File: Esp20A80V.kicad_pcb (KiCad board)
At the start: 2 copper layers, 75 x 29 mm, 19 parts, among them J1 dcdc, J4 I2C/Uart, Q1 SI2305, SW1 3x button, U1 tft + touch + sd card, U3 20A 80V dcdc, U4 Wemos S2 Mini

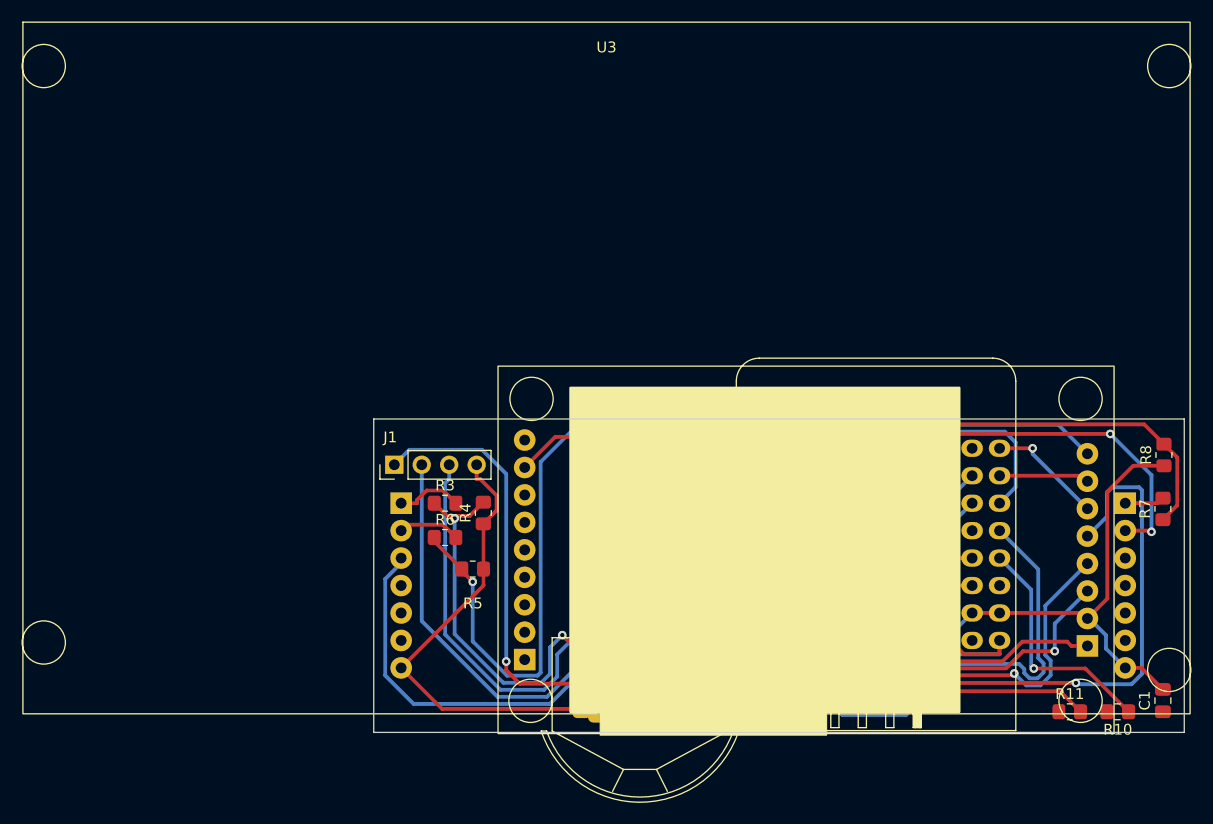
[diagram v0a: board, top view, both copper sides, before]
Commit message: footsprints verified and sd card added
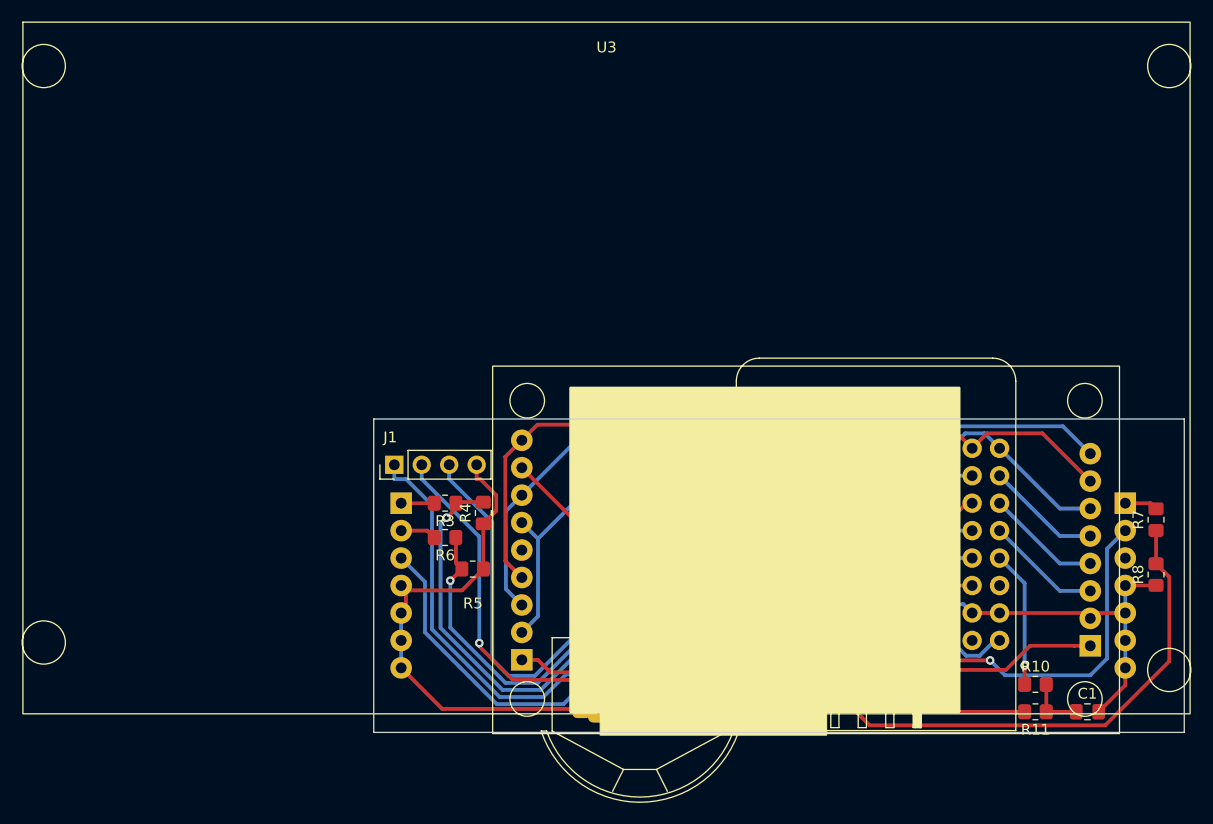
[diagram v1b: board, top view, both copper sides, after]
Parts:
- U1: value tft + touch + sd card -> spi tft with touch (+ sd card)
- moved Q1 27.5 mm to (152.7, 94.3), turned to 180 degrees
- moved R2 26.7 mm to (155.2, 97.8), turned to 180 degrees
- moved R1 19.1 mm to (148.6, 94.0), turned to -90 degrees
- moved R8 11.1 mm to (176.5, 101.6)
- moved R10 8.03 mm to (165.4, 111.8), turned to 0 degrees
- moved C1 7.06 mm to (170.2, 114.3), turned to 0 degrees
- moved R11 3.17 mm to (165.4, 114.3), turned to 180 degrees
- moved R7 1.18 mm to (176.5, 96.5)
- turned R3 to 180 degrees
- turned R6 to 180 degrees
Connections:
- net Net-(R7-Pad1) renamed iVout
- net Vin renamed Net-(U3-V_in)
- net Vout renamed Net-(U3-V_out)
- R2 pad 1: Net-(R2-Pad1) -> led
- R3 pad 1: Net-(R3-Pad1) -> enable
- R3 pad 2: enable -> Net-(U3-enable)
- R4 pad 2: Net-(R3-Pad1) -> enable
- R5 pad 2: Net-(R5-Pad2) -> iVin
- R6 pad 1: Net-(R5-Pad2) -> iVin
- SW1 pad 1: Net-(SW1-up) -> up
- SW1 pad 2: Net-(SW1-push) -> push
- SW1 pad 3: Net-(SW1-down) -> down
- U1 pad 10: unconnected-(U1-SD_MOSI-Pad10) -> MISO
- U1 pad 11: unconnected-(U1-SD_MISO-Pad11) -> MOSI
- U1 pad 12: unconnected-(U1-SD_SCK-Pad12) -> SCK
- U1 pad 14: unconnected-(U1-T_DO-Pad14) -> MISO
- U1 pad 15: unconnected-(U1-T_DIN-Pad15) -> MOSI
- U1 pad 16: Net-(U1-T_CS) -> T_CS
- U1 pad 17: unconnected-(U1-T_CLK-Pad17) -> SCK
- U1 pad 3: Net-(U1-CS) -> CS
- U1 pad 4: Net-(U1-RESET) -> RESET
- U1 pad 5: Net-(U1-A0) -> A0
- U1 pad 6: Net-(U1-SDA) -> MOSI
- U1 pad 7: Net-(U1-SCK) -> SCK
- U1 pad 9: unconnected-(U1-SD_CS-Pad9) -> SD_CS
- U3 pad 1: enable -> Net-(U3-enable)
- U3 pad 11: unconnected-(U3-GND-Pad11) -> GND
- U3 pad 12: unconnected-(U3-GND-Pad12) -> GND
- U3 pad 13: unconnected-(U3-GND-Pad13) -> GND
- U3 pad 4: unconnected-(U3-GND-Pad4) -> GND
- U3 pad 5: unconnected-(U3-GND-Pad5) -> GND
- U3 pad 6: unconnected-(U3-GND-Pad6) -> GND
- U4 pad 1: Net-(R5-Pad2) -> unconnected-(U4-Pad1)
- U4 pad 10: Net-(SW1-up) -> unconnected-(U4-Pad10)
- U4 pad 11: Net-(U1-CS) -> push
- U4 pad 12: Net-(R2-Pad1) -> up
- U4 pad 13: Net-(SW1-push) -> SD_CS
- U4 pad 14: Net-(SW1-down) -> mode
- U4 pad 21: mode -> SDA
- U4 pad 3: unconnected-(U4-Pad3) -> iVin
- U4 pad 33: Net-(R3-Pad1) -> CS
- U4 pad 34: unconnected-(U4-Pad34) -> SCL
- U4 pad 35: Net-(U1-T_CS) -> RESET
- U4 pad 36: SDA -> led
- U4 pad 37: Net-(U1-SCK) -> A0
- U4 pad 38: SCL -> MISO
- U4 pad 39: Net-(U1-SDA) -> MOSI
- U4 pad 40: unconnected-(U4-Pad40) -> SCK
- U4 pad 5: unconnected-(U4-Pad5) -> enable
- U4 pad 7: Net-(U1-A0) -> T_CS
- U4 pad 9: Net-(U1-RESET) -> down
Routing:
- net Net-(R3-Pad1): track 97.6 -> 0.00 mm, vias 3 -> 0
- net Net-(U1-A0): track 78.3 -> 0.00 mm, vias 1 -> 0
- net MOSI: track 0.00 -> 70.9 mm
- net SCK: track 0.00 -> 70.5 mm
- net Net-(R5-Pad2): track 62.6 -> 0.00 mm, vias 2 -> 0
- net MISO: track 0.00 -> 57.3 mm
- net Net-(U1-T_CS): track 54.3 -> 0.00 mm, vias 1 -> 0
- net Net-(U1-RESET): track 53.2 -> 0.00 mm, vias 1 -> 0
- net iVin: track 0.00 -> 47.0 mm, vias 0 -> 1
- net enable: track 6.21 -> 53.1 mm, vias 0 -> 1
- net Net-(U1-CS): track 44.0 -> 0.00 mm, vias 1 -> 0
- net Net-(Q1-S): track 51.7 -> 20.9 mm
- net SD_CS: track 0.00 -> 30.5 mm, vias 0 -> 1
- net iVout: track 46.3 -> 74.7 mm, vias 0 -> 1
- net mode: track 82.3 -> 54.3 mm, vias 3 -> 0
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
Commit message: better circuit
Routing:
- net GND: track 118.4 -> 146.1 mm
- net iVout: track 74.7 -> 47.6 mm, vias 1 -> 0
- net enable: track 53.1 -> 36.0 mm, vias 1 -> 0
- net +5V: track 96.6 -> 102.8 mm
- net SCK: track 70.5 -> 75.7 mm
- net MISO: track 57.3 -> 62.5 mm
- net DAC in: track 64.3 -> 61.8 mm
- net mode: track 54.3 -> 52.1 mm
- net Iout: track 54.4 -> 55.7 mm, vias 1 -> 0
- net Net-(U1-VCC): track 33.3 -> 32.2 mm
- net Net-(Q1-S): track 20.9 -> 20.1 mm, vias 1 -> 0
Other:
- board size 75 x 29 mm -> 75 x 30 mm

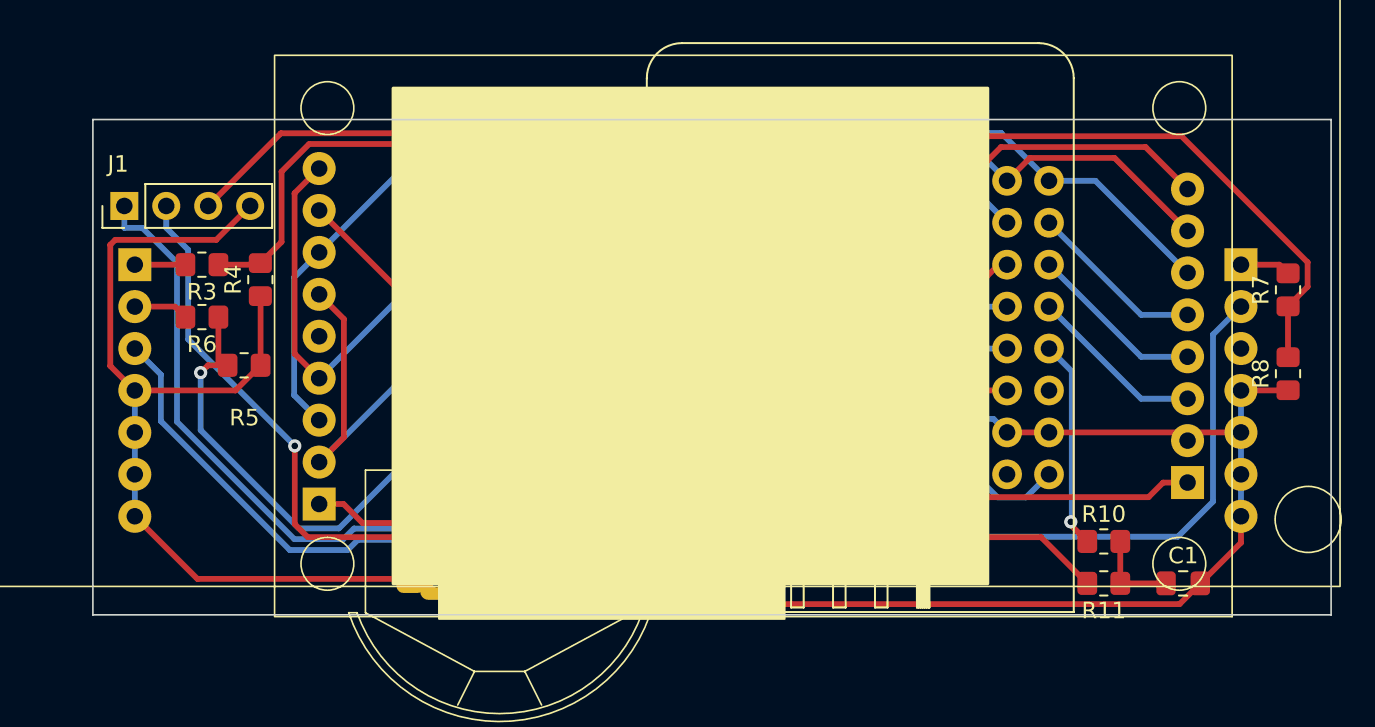
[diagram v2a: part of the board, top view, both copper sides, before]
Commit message: jst ph2.0 instead of dupont female
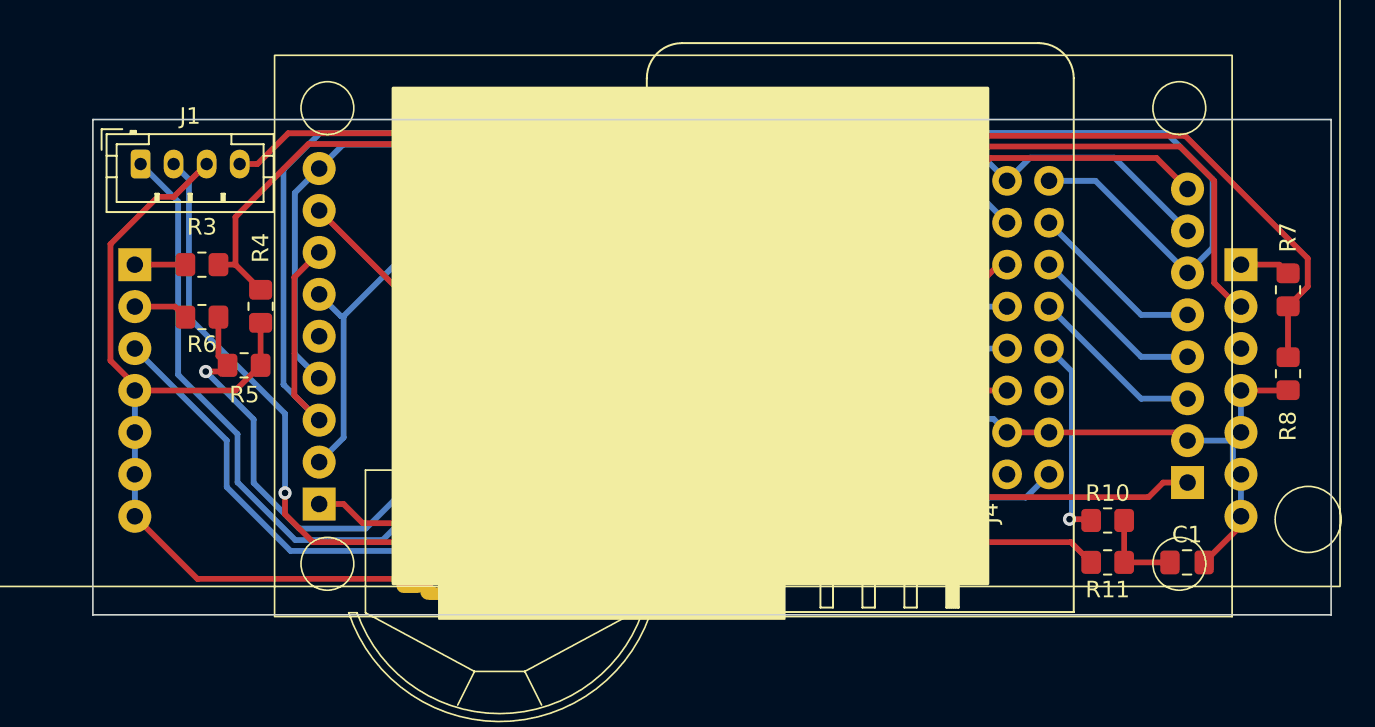
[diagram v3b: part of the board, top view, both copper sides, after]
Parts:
- added J2: free, Connector_PinHeader_2.54mm:PinHeader_1x06_P2.54mm_Horizontal, F.Cu at (144.8, 106.7)
- J1: footprint Connector_PinHeader_2.54mm:PinHeader_1x04_P2.54mm_Vertical -> Connector_JST:JST_PH_B4B-PH-K_1x04_P2.00mm_Vertical
- moved J1 2.72 mm to (107.0, 88.9), turned to 0 degrees
- moved J4 1.78 mm to (156.2, 105.7)
- moved R4 1.62 mm to (114.3, 97.5)
- moved R10 1.29 mm to (165.6, 110.5)
- moved C1 1.29 mm to (170.4, 113.0)
- moved R11 1.29 mm to (165.6, 113.0)
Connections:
- net DAC in renamed DAC_in
- net Net-(U1-VCC) renamed 3.3V
- J1 pad 3: +5V -> GND
- J1 pad 4: GND -> +5V
- U4 pad 1: unconnected-(U4-Pad1) -> iVout
- U4 pad 10: unconnected-(U4-Pad10) -> F1
- U4 pad 2: iVout -> Iout
- U4 pad 4: Iout -> F4
- U4 pad 6: unconnected-(U4-Pad6) -> F3
- U4 pad 8: unconnected-(U4-Pad8) -> F2
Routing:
- net +5V: track 102.8 -> 68.2 mm, vias 1 -> 0
- net MOSI: track 70.5 -> 102.8 mm
- net Iout: track 55.7 -> 41.5 mm, vias 0 -> 1
- net GND: track 146.1 -> 134.1 mm
- net SCK: track 75.7 -> 70.5 mm
- net MISO: track 62.5 -> 57.3 mm
- net F3: track 0.00 -> 3.47 mm
- net F1: track 0.00 -> 3.47 mm
- net F4: track 0.00 -> 3.47 mm
- net F2: track 0.00 -> 3.47 mm
- net 3.3V: track 32.2 -> 34.9 mm
- net DAC_out: track 72.0 -> 74.0 mm
- net SDA: track 12.5 -> 10.7 mm
- net SCL: track 16.1 -> 14.3 mm
- net mode: track 52.1 -> 53.6 mm, vias 0 -> 1
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
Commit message: update
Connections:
- J1 pad 1: mode -> DAC_out
- J1 pad 2: DAC_out -> mode
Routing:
- net GND: track 134.1 -> 0.00 mm
- net MOSI: track 102.8 -> 0.00 mm
- net DAC_out: track 74.0 -> 0.00 mm, vias 1 -> 0
- net SCK: track 70.5 -> 0.00 mm
- net +5V: track 68.2 -> 0.00 mm
- net DAC_in: track 60.4 -> 0.00 mm, vias 1 -> 0
- net MISO: track 57.3 -> 0.00 mm
- net mode: track 53.6 -> 0.00 mm, vias 1 -> 0
- net iVin: track 46.7 -> 0.00 mm, vias 1 -> 0
- net iVout: track 46.7 -> 0.00 mm, vias 1 -> 0
- net Iout: track 41.5 -> 0.00 mm, vias 1 -> 0
- net enable: track 37.3 -> 0.00 mm
- net 3.3V: track 34.9 -> 0.00 mm
- net SD_CS: track 30.4 -> 0.00 mm
- net T_CS: track 23.8 -> 0.00 mm
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
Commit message: update
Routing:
- net GND: track 0.00 -> 133.9 mm
- net MOSI: track 0.00 -> 111.4 mm, vias 0 -> 1
- net +5V: track 0.00 -> 98.4 mm, vias 0 -> 1
- net DAC_out: track 0.00 -> 83.0 mm
- net SCK: track 0.00 -> 74.5 mm
- net DAC_in: track 0.00 -> 60.1 mm, vias 0 -> 1
- net MISO: track 0.00 -> 57.9 mm
- net iVin: track 0.00 -> 47.8 mm, vias 0 -> 1
- net iVout: track 0.00 -> 46.7 mm
- net mode: track 0.00 -> 43.5 mm, vias 0 -> 1
- net Iout: track 0.00 -> 41.5 mm
- net enable: track 0.00 -> 37.8 mm
- net 3.3V: track 0.00 -> 34.9 mm
- net SD_CS: track 0.00 -> 31.1 mm
- net T_CS: track 0.00 -> 23.9 mm
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
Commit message: update
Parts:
- added R12: 99k, Resistor_SMD:R_0805_2012Metric_Pad1.20x1.40mm_HandSolder, F.Cu at (146.3, 90.2)
- added R13: 1k, Resistor_SMD:R_0805_2012Metric_Pad1.20x1.40mm_HandSolder, F.Cu at (151.4, 90.2)
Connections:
- U3 pad 9: Iout -> Net-(U3-I_out)
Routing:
- net Iout: track 41.5 -> 10.6 mm
- net Net-(U3-I_out): track 0.00 -> 29.9 mm
- net 3.3V: track 34.9 -> 56.3 mm, vias 0 -> 2
- net MOSI: track 111.4 -> 93.9 mm
- net mode: track 43.5 -> 57.9 mm
- net +5V: track 98.4 -> 111.0 mm, vias 1 -> 2
- net DAC_in: track 60.1 -> 72.6 mm, vias 1 -> 0
- net GND: track 133.9 -> 126.5 mm
- net SCK: track 74.5 -> 70.4 mm
- net Net-(R10-Pad1): track 12.3 -> 11.5 mm
- net MISO: track 57.9 -> 57.3 mm
- net DAC_out: track 83.0 -> 83.3 mm, vias 0 -> 1

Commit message: update
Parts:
- moved R8 10.8 mm to (175.9, 90.8)
- moved R7 6.54 mm to (173.4, 90.8), turned to -90 degrees
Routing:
- net +5V: track 111.0 -> 130.9 mm, vias 2 -> 0
- net GND: track 126.5 -> 143.8 mm
- net DAC_in: track 72.6 -> 60.2 mm, vias 0 -> 1
- net iVout: track 46.7 -> 35.8 mm
- net DAC_out: track 83.3 -> 75.4 mm
- net MOSI: track 93.9 -> 100.4 mm
- net mode: track 57.9 -> 52.8 mm, vias 1 -> 0
- net 3.3V: track 56.3 -> 53.6 mm, vias 2 -> 0
- net iVin: track 47.6 -> 46.5 mm
- net Net-(R10-Pad1): track 11.5 -> 12.1 mm
- net SD_CS: track 31.1 -> 31.8 mm, vias 0 -> 1
- net Net-(U3-I_out): vias 0 -> 1

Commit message: update
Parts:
- moved R7 3.20 mm to (173.0, 87.6), turned to 0 degrees
- moved R8 2.54 mm to (173.4, 90.8)
- moved R1 1.55 mm to (149.9, 94.9)
- moved Q1 1.27 mm to (154.0, 94.3)
- moved R9 1.09 mm to (155.8, 101.6)
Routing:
- net +5V: track 130.9 -> 92.2 mm, vias 0 -> 1
- net iVout: track 35.8 -> 2.74 mm
- net MOSI: track 100.4 -> 73.5 mm, vias 1 -> 2
- net mode: track 52.8 -> 44.0 mm, vias 0 -> 1
- net DAC_out: track 75.4 -> 83.1 mm
- net GND: track 143.8 -> 150.4 mm
- net DAC_in: track 60.2 -> 66.4 mm, vias 1 -> 2
- net Net-(U3-V_out): track 3.33 -> 7.95 mm
- net SCK: track 70.4 -> 74.7 mm
- net Net-(Q1-G): track 7.94 -> 10.9 mm, vias 0 -> 2
- net iVin: track 46.5 -> 48.3 mm, vias 1 -> 3
- net SD_CS: track 31.8 -> 30.4 mm, vias 1 -> 0
- net SDA: track 10.7 -> 11.5 mm
- net 3.3V: track 53.6 -> 53.5 mm, vias 0 -> 1
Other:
- board size 75 x 30 mm -> 72 x 30 mm
